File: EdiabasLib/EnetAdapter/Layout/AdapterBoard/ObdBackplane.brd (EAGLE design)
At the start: 32 x 19.5 mm, 10 parts

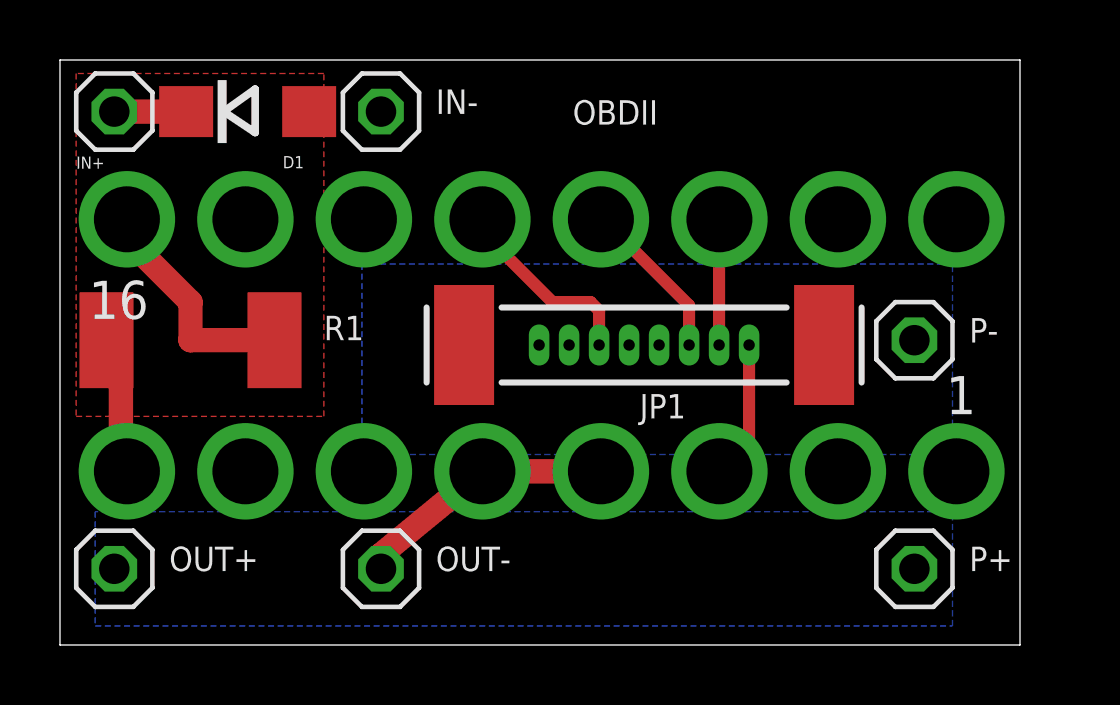
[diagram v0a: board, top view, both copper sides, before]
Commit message: Added new solder pad
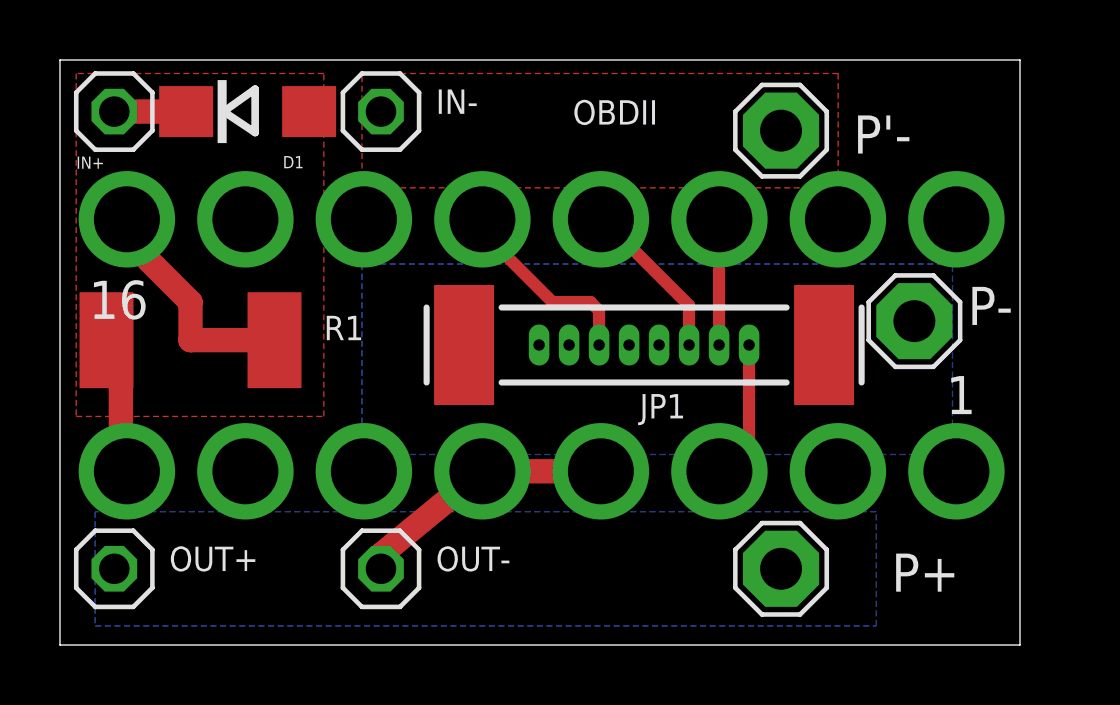
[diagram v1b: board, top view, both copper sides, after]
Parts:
- added P'-: SE14, solpad:SE14
- P+: value 5V -> SE14; device pinhead:1X01 -> solpad:SE14
- P-: value GND -> SE14; device pinhead:1X01 -> solpad:SE14
- moved P+ 4.45 mm to (26.0, 2.54)
- moved P- 0.63 mm to (30.5, 10.8)
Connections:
- new net GND2: IN-.1, P'-.MP
- net +5V: now also P+.MP; no longer P+.1
- net GND: now also P-.MP; no longer P-.1
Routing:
- added copper zone on layer 1, net GND2
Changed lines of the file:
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@@
 <attribute name="VALUE" x="10.795" y="8.89" size="0.8128" layer="27"/>
-</element>
-<element name="P+" library="pinhead" package="1X01" value="5V" x="30.48" y="2.54" smashed="yes">
-<attribute name="NAME" x="32.3088" y="2.4638" size="0.8128" layer="25" ratio="10"/>
-<attribute name="VALUE" x="32.385" y="1.27" size="0.8128" layer="27"/>
-</element>
-<element name="P-" library="pinhead" package="1X01" value="GND" x="30.48" y="10.16" smashed="yes">
-<attribute name="NAME" x="32.3088" y="10.0838" size="0.8128" layer="25" ratio="10"/>
-<attribute name="VALUE" x="31.75" y="8.89" size="0.8128" layer="27"/>
 </element>
 <element name="JP1" library="obd_special" package="1X08M-1MM" value="ETHERNET" x="21.47" y="10" smashed="yes">
 <attribute name="NAME" x="22.86" y="8.365" size="0.8128" layer="25" ratio="14" rot="R180"/>
+</element>
+<element name="P+" library="solpad" package="SE14" value="SE14" x="26.035" y="2.54" smashed="yes">
+<attribute name="NAME" x="29.718" y="1.778" size="1.27" layer="25" ratio="10"/>
+</element>
+<element name="P-" library="solpad" package="SE14" value="SE14" x="30.48" y="10.795" smashed="yes">
+<attribute name="NAME" x="32.258" y="10.668" size="1.27" layer="25" ratio="10"/>
+</element>
+<element name="P'-" library="solpad" package="SE14" value="SE14" x="26.035" y="17.145" smashed="yes">
+<attribute name="NAME" x="28.448" y="16.383" size="1.27" layer="25" ratio="10"/>
 </element>
 </elements>
@@
 <contactref element="OBDII" pad="4"/>
 <contactref element="OUT-" pad="1"/>
-<contactref element="P-" pad="1"/>
 <wire x1="12.7" y1="2.54" x2="12.7" y2="3.01" width="0.8128" layer="1"/>
 <wire x1="12.7" y1="3.01" x2="16.08" y2="5.79" width="0.8128" layer="1"/>
@@
 <vertex x="12.065" y="6.35"/>
 </polygon>
+<contactref element="P-" pad="MP"/>
 </signal>
 <signal name="+12V">
@@
 <signal name="+5V">
 <contactref element="OUT+" pad="1"/>
-<contactref element="P+" pad="1"/>
 <polygon width="0.254" layer="16" spacing="0.254" isolate="0.4064">
 <vertex x="3.175" y="0.635"/>
-<vertex x="31.75" y="0.635"/>
-<vertex x="31.75" y="4.445"/>
+<vertex x="29.21" y="0.635"/>
+<vertex x="29.21" y="4.445"/>
 <vertex x="3.175" y="4.445"/>
 </polygon>
+<contactref element="P+" pad="MP"/>
 </signal>
 <signal name="N$3">
@@
 <wire x1="20.25" y1="13.97" x2="20.03" y2="14.19" width="0.4064" layer="1"/>
 </signal>
+<signal name="GND2">
+<contactref element="IN-" pad="1"/>
+<contactref element="P'-" pad="MP"/>
+<polygon width="0.254" layer="1" spacing="0.254" isolate="0.4064">
+<vertex x="12.065" y="19.05"/>
+<vertex x="27.94" y="19.05"/>
+<vertex x="27.94" y="15.24"/>
+<vertex x="12.065" y="15.24"/>
+</polygon>
+</signal>
 </signals>

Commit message: Updated to eagle 8.3.2
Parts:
- D1: value (none) -> 100V
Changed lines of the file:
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@@
 <?xml version="1.0" encoding="utf-8"?>
 <!DOCTYPE eagle SYSTEM "eagle.dtd">
-<eagle version="7.7.0">
+<eagle version="8.3.2">
 <drawing>
 <settings>
 <setting alwaysvectorfont="no"/>
+<setting keepoldvectorfont="yes"/>
 <setting verticaltext="up"/>
 </settings>
@@
 <layer number="230" name="230bmp" color="7" fill="1" visible="yes" active="yes"/>
 <layer number="231" name="231bmp" color="7" fill="1" visible="yes" active="yes"/>
+<layer number="232" name="Eagle3D_PG2" color="7" fill="1" visible="yes" active="yes"/>
+<layer number="233" name="Eagle3D_PG3" color="7" fill="1" visible="yes" active="yes"/>
 <layer number="248" name="Housing" color="7" fill="1" visible="yes" active="yes"/>
 <layer number="249" name="Edge" color="7" fill="1" visible="yes" active="yes"/>
@@
 </autorouter>
 <elements>
-<element name="D1" library="diode" package="DO214AC" value="" x="8.255" y="17.78" smashed="yes">
+<element name="D1" library="diode" library_urn="urn:adsk.eagle:library:210" package="DO214AC" package3d_urn="urn:adsk.eagle:package:43417/2" value="100V" x="8.255" y="17.78" smashed="yes">
 <attribute name="NAME" x="9.425" y="15.891" size="0.4064" layer="25" ratio="10"/>
-<attribute name="VALUE" x="5.615" y="15.224" size="1.27" layer="27" ratio="10"/>
-</element>
-<element name="IN+" library="pinhead" package="1X01" value="12V" x="3.81" y="17.78" smashed="yes">
+<attribute name="VALUE" x="5.615" y="15.859" size="0.508" layer="27" ratio="10"/>
+</element>
+<element name="IN+" library="pinhead" library_urn="urn:adsk.eagle:library:325" package="1X01" package3d_urn="urn:adsk.eagle:package:22485/2" value="12V" x="3.81" y="17.78" smashed="yes">
 <attribute name="NAME" x="2.54" y="15.875" size="0.4064" layer="25" ratio="10"/>
 </element>
-<element name="IN-" library="pinhead" package="1X01" value="GND" x="12.7" y="17.78" smashed="yes">
+<element name="IN-" library="pinhead" library_urn="urn:adsk.eagle:library:325" package="1X01" package3d_urn="urn:adsk.eagle:package:22485/2" value="GND" x="12.7" y="17.78" smashed="yes">
 <attribute name="NAME" x="14.5288" y="17.7038" size="0.8128" layer="25" ratio="10"/>
 <attribute name="VALUE" x="14.605" y="16.51" size="0.8128" layer="27"/>
 </element>
-<element name="OBDII" library="SparkFun-Connectors" package="OBDII" value="OBDII" x="18.2" y="9.6" smashed="yes">
+<element name="OBDII" library="SparkFun-Connectors" library_urn="urn:adsk.eagle:library:513" package="OBDII" package3d_urn="urn:adsk.eagle:package:38217/1" value="OBDII" x="18.2" y="9.6" smashed="yes">
+<attribute name="NAME" x="19.089" y="17.347" size="0.8128" layer="25" font="vector" ratio="20"/>
 <attribute name="SF_ID" value="DEV-09911" x="18.2" y="9.6" size="1.778" layer="27" display="off"/>
-<attribute name="NAME" x="19.089" y="17.347" size="0.8128" layer="25" font="vector" ratio="20"/>
-</element>
-<element name="OUT+" library="pinhead" package="1X01" value="5V" x="3.81" y="2.54" smashed="yes">
+</element>
+<element name="OUT+" library="pinhead" library_urn="urn:adsk.eagle:library:325" package="1X01" package3d_urn="urn:adsk.eagle:package:22485/2" value="5V" x="3.81" y="2.54" smashed="yes">
 <attribute name="NAME" x="5.6388" y="2.4638" size="0.8128" layer="25" ratio="10"/>
 <attribute name="VALUE" x="5.715" y="1.27" size="0.8128" layer="27"/>
 </element>
-<element name="OUT-" library="pinhead" package="1X01" value="GND" x="12.7" y="2.54" smashed="yes">
+<element name="OUT-" library="pinhead" library_urn="urn:adsk.eagle:library:325" package="1X01" package3d_urn="urn:adsk.eagle:package:22485/2" value="GND" x="12.7" y="2.54" smashed="yes">
 <attribute name="NAME" x="14.5288" y="2.4638" size="0.8128" layer="25" ratio="10"/>
 <attribute name="VALUE" x="14.605" y="1.27" size="0.8128" layer="27"/>
 </element>
-<element name="R1" library="resistor" package="R2512" value="511" x="6.35" y="10.16" smashed="yes">
+<element name="R1" library="resistor" library_urn="urn:adsk.eagle:library:348" package="R2512" package3d_urn="urn:adsk.eagle:package:26070/1" value="511" x="6.35" y="10.16" smashed="yes">
 <attribute name="NAME" x="10.795" y="10.16" size="0.8128" layer="25"/>
 <attribute name="VALUE" x="10.795" y="8.89" size="0.8128" layer="27"/>
 </element>
 <element name="JP1" library="obd_special" package="1X08M-1MM" value="ETHERNET" x="21.47" y="10" smashed="yes">
-<attribute name="NAME" x="22.86" y="8.365" size="0.8128" layer="25" ratio="14" rot="R180"/>
-</element>
-<element name="P+" library="solpad" package="SE14" value="SE14" x="26.035" y="2.54" smashed="yes">
-<attribute name="NAME" x="29.718" y="1.778" size="1.27" layer="25" ratio="10"/>
-</element>
-<element name="P-" library="solpad" package="SE14" value="SE14" x="30.48" y="10.795" smashed="yes">
-<attribute name="NAME" x="32.258" y="10.668" size="1.27" layer="25" ratio="10"/>
-</element>
-<element name="P'-" library="solpad" package="SE14" value="SE14" x="26.035" y="17.145" smashed="yes">
-<attribute name="NAME" x="28.448" y="16.383" size="1.27" layer="25" ratio="10"/>
+<attribute name="NAME" x="22.225" y="8.365" size="0.508" layer="25" ratio="14" rot="R180"/>
+</element>
+<element name="P+" library="solpad" library_urn="urn:adsk.eagle:library:364" package="SE14" package3d_urn="urn:adsk.eagle:package:26504/1" value="SE14" x="26.035" y="2.54" smashed="yes">
+<attribute name="NAME" x="29.718" y="1.778" size="0.8128" layer="25" ratio="10"/>
+</element>
+<element name="P-" library="solpad" library_urn="urn:adsk.eagle:library:364" package="SE14" package3d_urn="urn:adsk.eagle:package:26504/1" value="SE14" x="30.48" y="10.795" smashed="yes">
+<attribute name="NAME" x="29.718" y="8.128" size="0.8128" layer="25" ratio="10"/>
+</element>
+<element name="P'-" library="solpad" library_urn="urn:adsk.eagle:library:364" package="SE14" package3d_urn="urn:adsk.eagle:package:26504/1" value="SE14" x="26.035" y="17.145" smashed="yes">
+<attribute name="NAME" x="28.448" y="16.383" size="0.8128" layer="25" ratio="10"/>
 </element>
 </elements>
@@
 </board>
 </drawing>
+<compatibility>
+<note version="8.2" severity="warning">
+Since Version 8.2, EAGLE supports online libraries. The ids
+of those online libraries will not be understood (or retained)
+with this version.
+</note>
+<note version="8.3" severity="warning">
+Since Version 8.3, EAGLE supports URNs for individual library
+assets (packages, symbols, and devices). The URNs of those assets
+will not be understood (or retained) with this version.
+</note>
+<note version="8.3" severity="warning">
+Since Version 8.3, EAGLE supports the association of 3D packages
+with devices in libraries, schematics, and board files. Those 3D
+packages will not be understood (or retained) with this version.
+</note>
+</compatibility>
 </eagle>
